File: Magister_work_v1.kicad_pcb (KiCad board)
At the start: 4 copper layers, 50.5 x 81 mm, 151 parts, among them J1 Conn_01x02_Pin, J10 Conn_01x06_Pin, J11 Conn_01x03_Pin, J12 Conn_01x03_Pin, J13 Conn_01x03_Pin, J14 Conn_01x03_Pin, J15 Conn_01x02_Pin, J17 Conn_01x04_Pin, J2 Conn_01x03_Pin, J3 Conn_01x03_Pin, J4 Conn_01x03_Pin, J5 Conn_01x03_Pin, J6 Conn_01x04_Pin, J7 Conn_01x02_Pin, J8 Conn_01x06_Pin, J9 Conn_01x02_Pin, Q1 AO3400A, Q2 AO3400A, U10 LSM6DS3, U11 MPU-6500, U12 BMI270, U2 XC6206P332MR, U3 Ai-Thinker-Ra-01, U4 MCP6001-OT, U5 AMS1117-3.3, U6 XL1509-5.0, U7 STM32F407VETx, U8 AT24C256, U9 Ai-Thinker-Ra-01SH, Y1 X322525MQB4SI, Y2 SMD03215C2

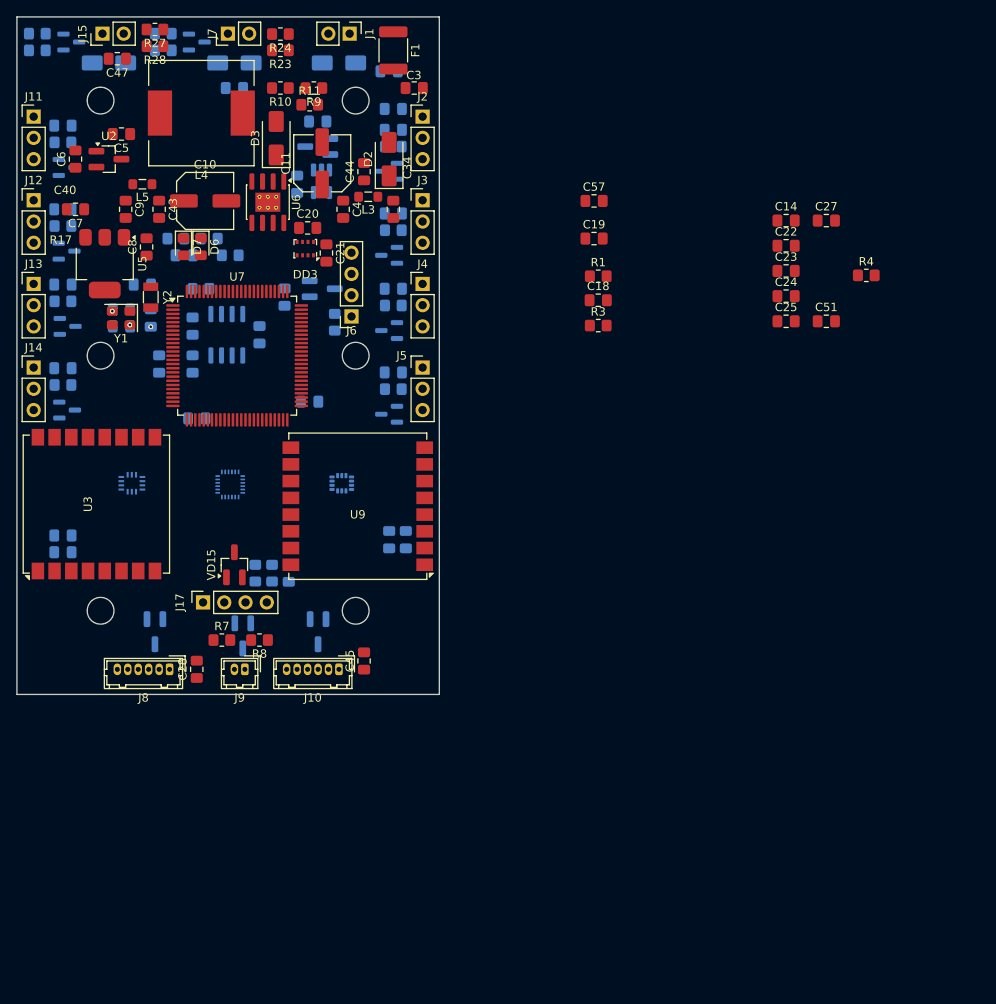
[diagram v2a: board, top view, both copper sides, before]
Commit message: feat: Разведены линии питания
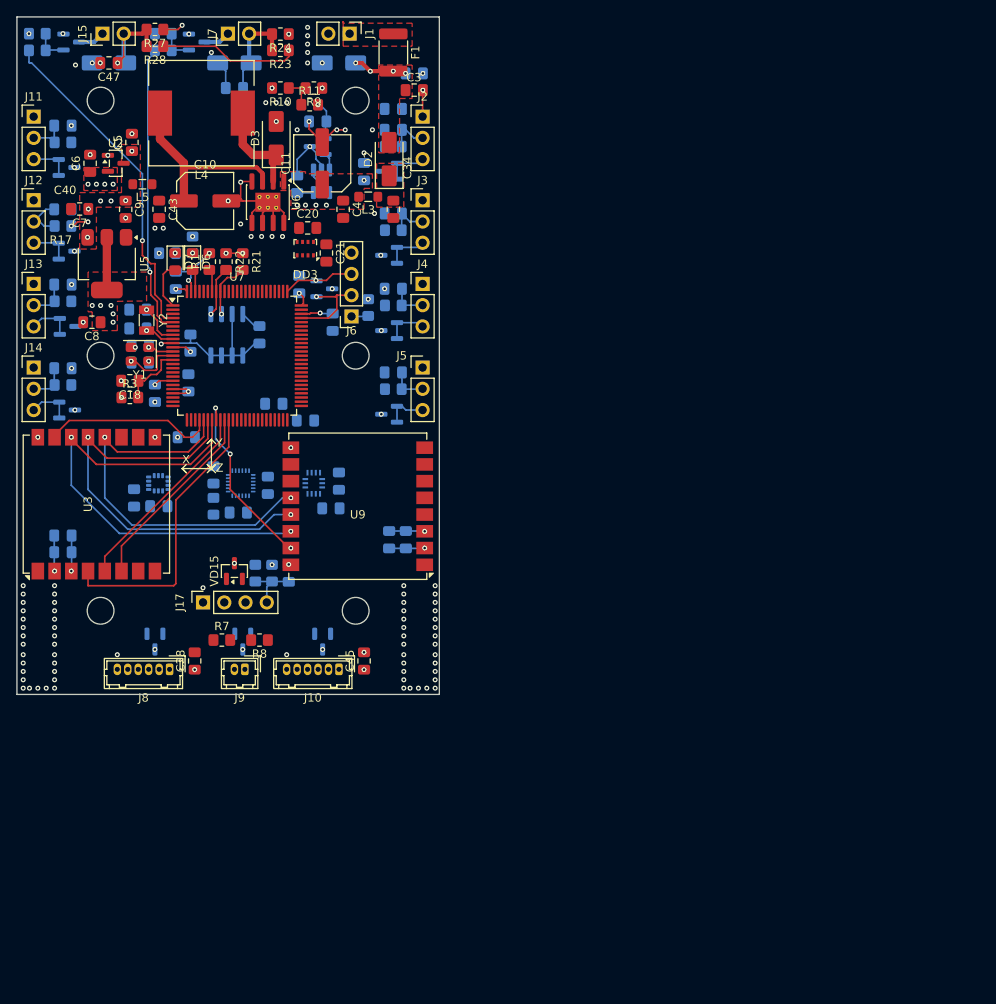
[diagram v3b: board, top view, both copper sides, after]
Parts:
- C14, C19, C22, C23, C24, C25, C27, C44, C51, C57, R4: moved to B.Cu
- R21, R22: moved to F.Cu
- U2, VD10, VD14, VD15, VD2, VD3, VD4: footprint Package_TO_SOT_SMD:SOT-23_Handsoldering -> Package_TO_SOT_SMD:SOT-23
- moved C22 83.6 mm to (44.0, 87.5), turned to -90 degrees
- moved R4 82.8 mm to (53.5, 88.5), turned to -90 degrees
- moved C23 80.1 mm to (47.0, 88.5)
- moved C25 70.9 mm to (53.5, 84.8), turned to 90 degrees
- moved C24 70.4 mm to (56.5, 89.2), turned to 180 degrees
- moved C14 69.6 mm to (60.0, 86.0), turned to 90 degrees
- moved C27 66.1 mm to (68.5, 85.5), turned to -90 degrees
- moved C51 63.3 mm to (67.5, 88.8), turned to 180 degrees
- moved C18 56.8 mm to (43.5, 73.5), turned to 180 degrees
- moved R3 56.7 mm to (43.5, 75.5)
- moved R1 46.5 mm to (53.0, 59.2), turned to 90 degrees
- moved C19 43.1 mm to (60.7, 76.2), turned to 180 degrees
- moved C57 34.5 mm to (67.8, 66.5), turned to -90 degrees
- moved U10 21.9 mm to (46.9, 85.8)
- moved U12 21.8 mm to (65.5, 85.8), turned to -90 degrees
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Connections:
- U6 pad 9: (no net) -> GND
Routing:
- net GND: track 0.00 -> 79.4 mm, vias 3 -> 133
- net MOSI_LoRa: track 0.00 -> 56.6 mm, vias 0 -> 2
- net MISO_LoRa: track 0.00 -> 51.9 mm, vias 0 -> 2
- net SCK_LoRa: track 0.00 -> 47.6 mm, vias 0 -> 2
- net POWER_DO2: track 0.00 -> 40.2 mm, vias 0 -> 1
- net +12V: track 0.00 -> 37.6 mm, vias 0 -> 7
- net +5V: track 0.00 -> 37.3 mm, vias 0 -> 13
- net POWER_DO1: track 0.00 -> 34.9 mm, vias 0 -> 1
- net Reset_LoRa: track 0.00 -> 34.5 mm
- net +3V3D: track 0.00 -> 27.3 mm, vias 0 -> 17
- net DIO0_LoRa: track 0.00 -> 23.8 mm
- net DIO1_LoRa: track 0.00 -> 23.2 mm
- net Net-(U6-FB): track 0.00 -> 22.9 mm
- net SS_RaSH: track 0.00 -> 22.1 mm, vias 0 -> 3
- net SS_LoRa: track 0.00 -> 20.8 mm
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- added copper zone on F.Cu, net +12V
- added copper zone on F.Cu, net +12V_1
- added copper zone on F.Cu, net +12V_in
- added copper zone on F.Cu, net +3V3A
- added copper zone on F.Cu, net +3V3D
- added copper zone on F.Cu, net +5V
- added copper zone on F.Cu, net Net-(D2-K)
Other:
- board text added: "X"
- board text added: "Y"
- board text added: "Z"

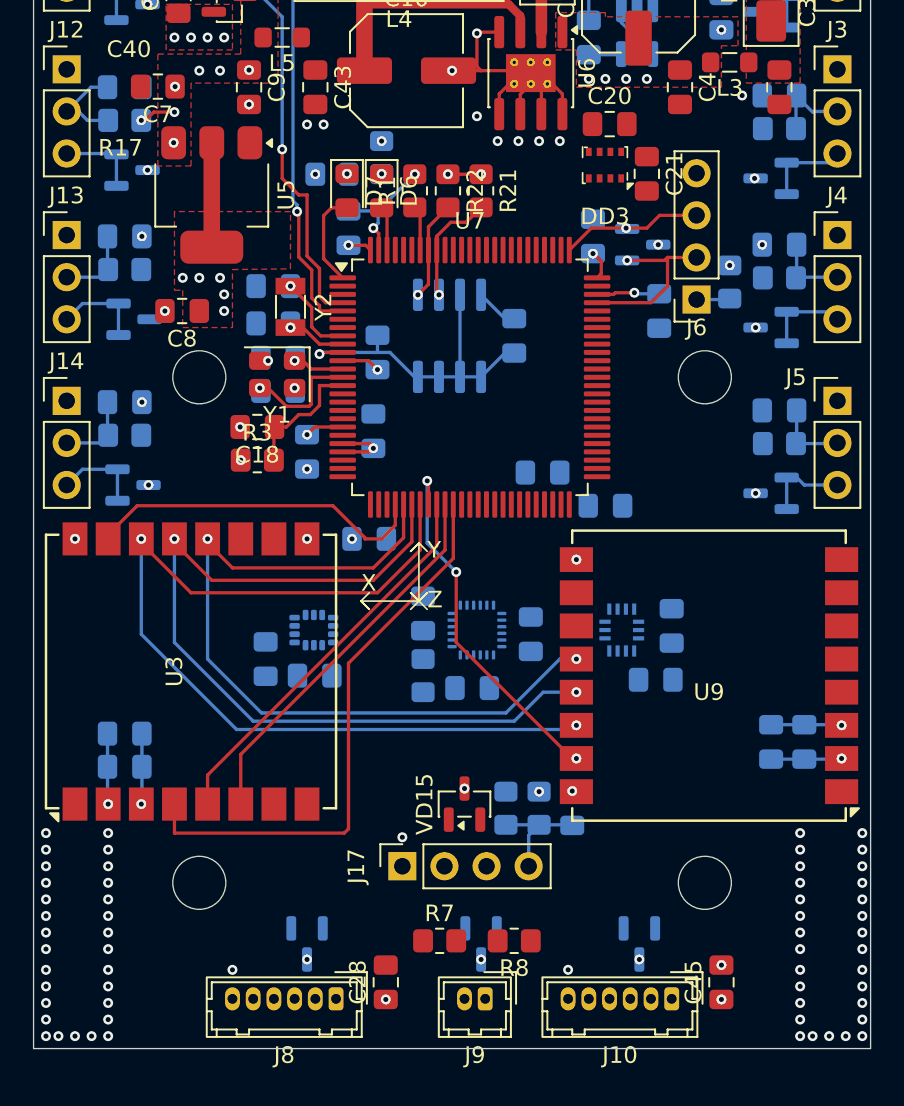
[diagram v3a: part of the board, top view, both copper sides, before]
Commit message: feat: разведены линии для датчиков LSM и BMP280
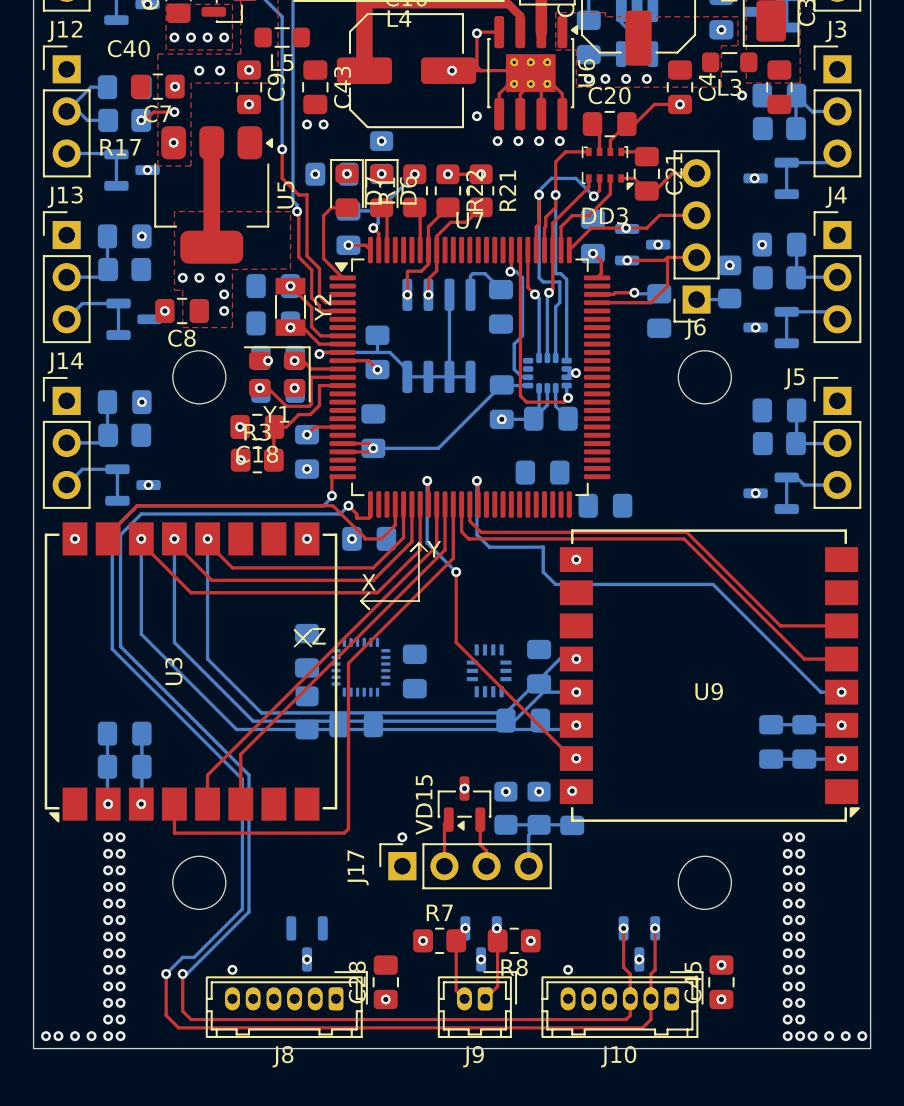
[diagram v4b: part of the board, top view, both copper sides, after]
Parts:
- moved C22 21.1 mm to (58.2, 72.0)
- moved C23 21.1 mm to (61.2, 73.0)
- moved U10 20.9 mm to (61.0, 70.2)
- moved C27 8.37 mm to (60.5, 88.0)
- moved U12 8.37 mm to (57.5, 88.2)
- moved C51 8.37 mm to (59.5, 91.2)
- moved C14 7.35 mm to (53.0, 88.2)
- moved C24 7.35 mm to (49.5, 91.5)
- moved C25 7.35 mm to (46.5, 87.0)
- moved R4 7.35 mm to (46.5, 90.8)
- moved U11 7.35 mm to (49.8, 88.0)
- moved C31 1.92 mm to (58.2, 66.2)
- moved U8 0.64 mm to (54.5, 68.0)
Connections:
- U6 pad 9: GND -> (no net)
- U7 pad 18: unconnected-(U7-PC3-Pad18) -> BAT_CTRL
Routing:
- net DEBUG_TX1: track 0.00 -> 86.2 mm, vias 0 -> 3
- net DEBUG_RX1: track 0.00 -> 83.5 mm, vias 0 -> 3
- net Reset_RaSH: track 0.00 -> 31.5 mm, vias 0 -> 2
- net DIO0_RaSH: track 0.00 -> 27.8 mm
- net DIO1_RaSH: track 0.00 -> 26.0 mm
- net LSM_SDI: track 0.00 -> 20.0 mm, vias 0 -> 2
- net LSM_SDO: track 0.00 -> 18.3 mm, vias 0 -> 1
- net GND: track 79.4 -> 95.3 mm, vias 133 -> 138
- net LSM_INT1: track 0.00 -> 12.7 mm, vias 0 -> 1
- net +3V3A: track 5.91 -> 18.5 mm
- net LSM_SCLK: track 0.00 -> 11.9 mm, vias 0 -> 1
- net LSM_INT2: track 0.00 -> 8.98 mm, vias 0 -> 1
- net LSM_CS: track 0.00 -> 6.79 mm, vias 0 -> 1
- net CSB_BMP280: track 0.00 -> 6.14 mm
- net +3V3D: track 27.3 -> 32.2 mm, vias 17 -> 20
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
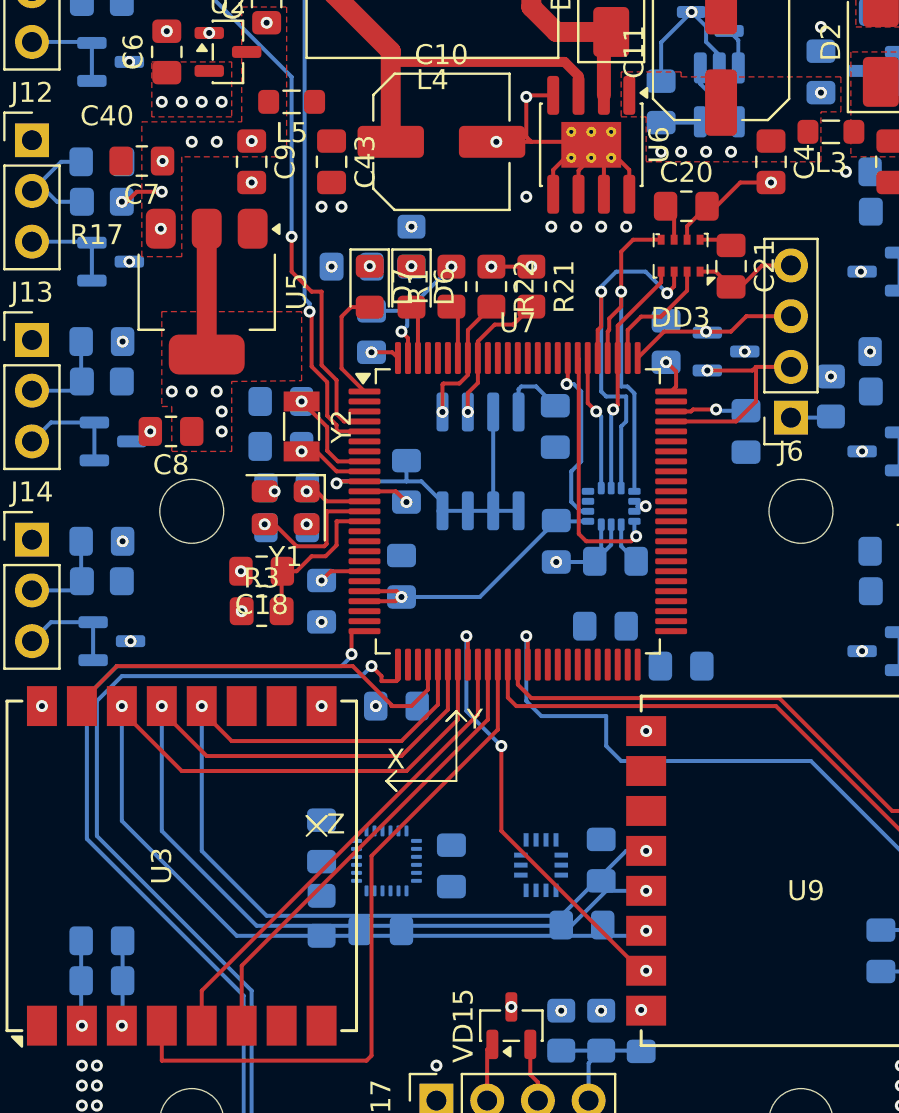
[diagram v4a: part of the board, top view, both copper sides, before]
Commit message: feat: Проведены цифровые линии от датчиков IMU
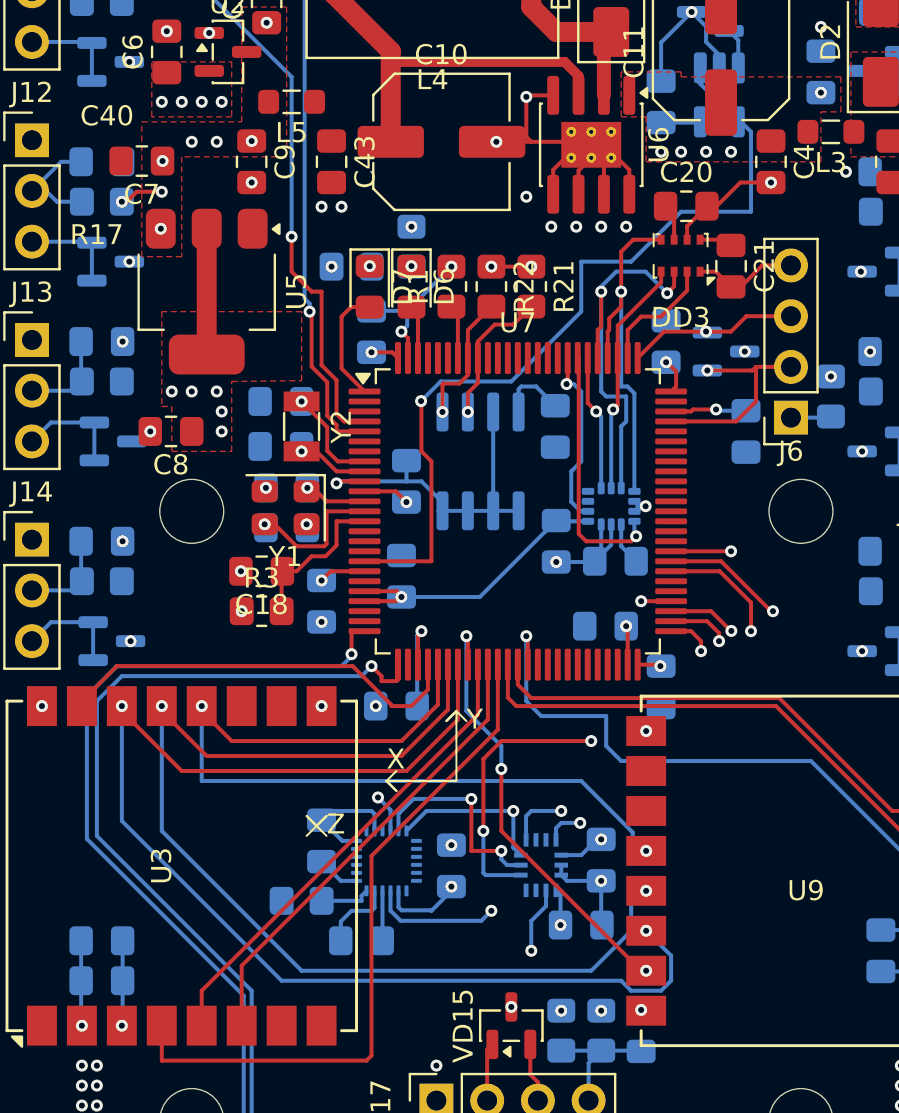
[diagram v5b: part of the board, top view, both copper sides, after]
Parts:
- moved C16 1.44 mm to (63.5, 79.3), turned to -90 degrees
- moved R4 1.25 mm to (45.5, 90.0), turned to 180 degrees
- moved C24 1.08 mm to (48.5, 92.0)
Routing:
- net MPU_CS: track 0.00 -> 48.0 mm, vias 0 -> 2
- net BAT_CTRL: track 3.49 -> 41.8 mm, vias 0 -> 1
- net BMI270_INT2: track 0.00 -> 36.8 mm, vias 0 -> 2
- net BMI270_SDO: track 0.00 -> 34.3 mm, vias 0 -> 3
- net BMI270_SCLK: track 0.00 -> 30.8 mm, vias 0 -> 3
- net BMI270_CS: track 0.00 -> 24.1 mm, vias 0 -> 3
- net BMI270_SDI: track 0.00 -> 23.7 mm, vias 0 -> 2
- net BMI270_INT1: track 0.00 -> 22.9 mm, vias 0 -> 2
- net GND: track 95.3 -> 109.9 mm, vias 138 -> 140
- net +3V3D: track 32.2 -> 45.4 mm, vias 20 -> 24
- net MOSI_LoRa: track 56.6 -> 62.1 mm
- net SCK_LoRa: track 47.6 -> 43.0 mm
- net +3V3A: track 18.5 -> 22.5 mm, vias 5 -> 6
- net MISO_LoRa: track 51.9 -> 54.7 mm
- net MPU_INT: track 0.00 -> 2.60 mm
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
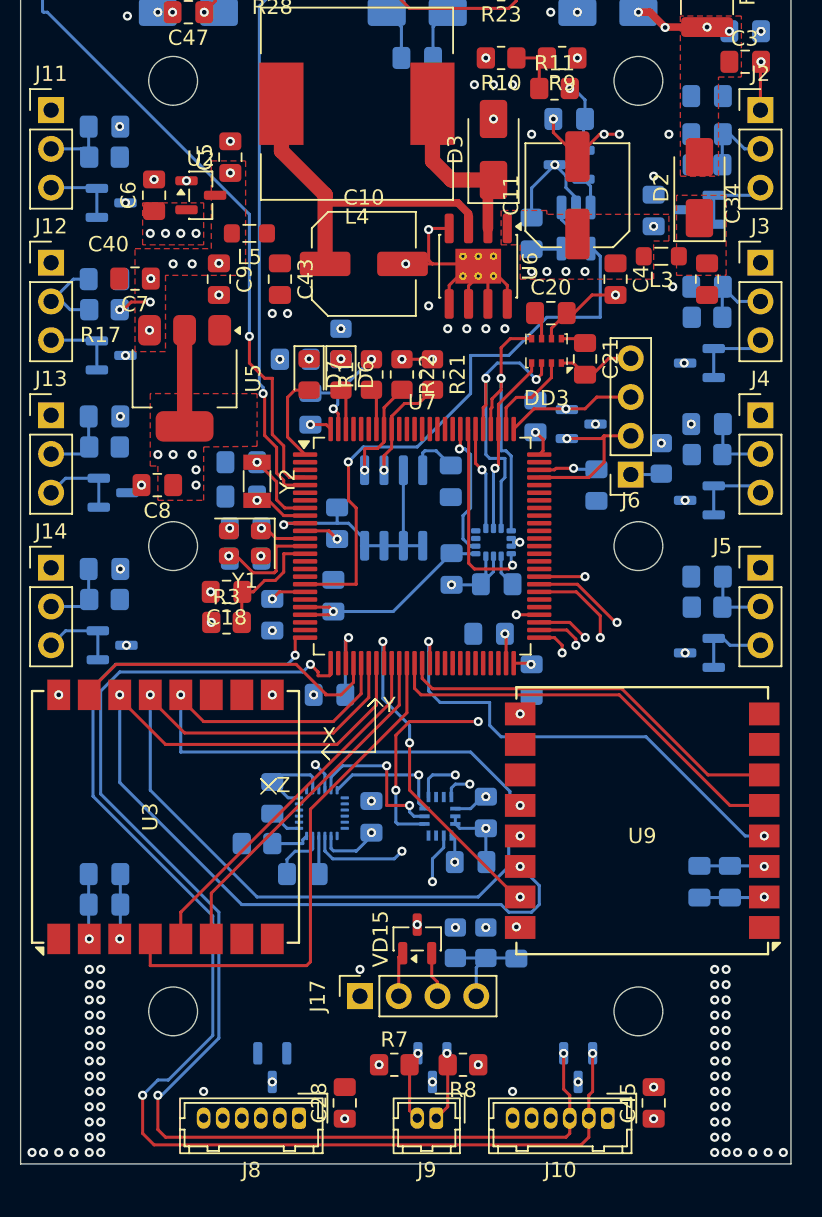
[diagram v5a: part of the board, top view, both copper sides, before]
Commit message: feat: Проведены линии для внешнего отладочного порта и внешенего компаса, провдена перекомпоновка разъёмов
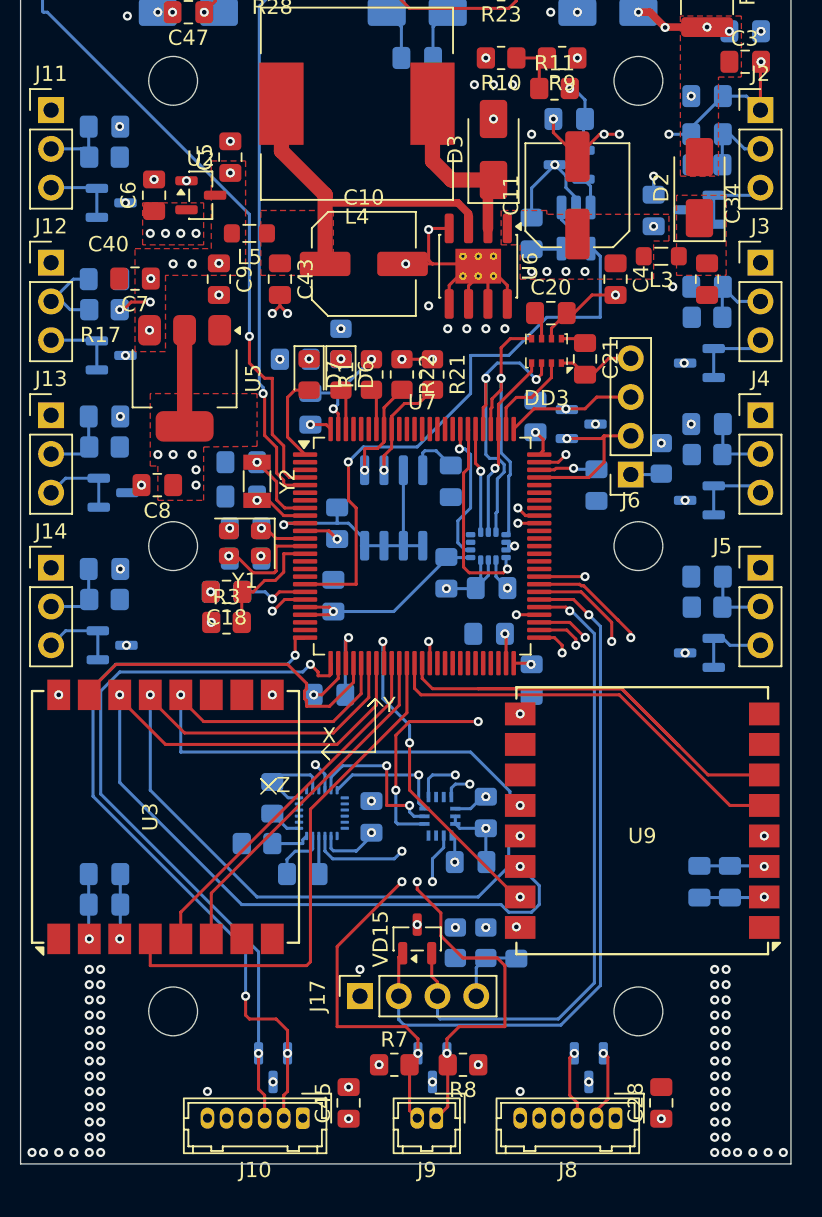
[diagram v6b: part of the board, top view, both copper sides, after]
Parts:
- moved C28 20.8 mm to (72.0, 107.0)
- moved J8 20.8 mm to (69.0, 108.0)
- moved VD2 20.8 mm to (67.2, 104.7)
- moved C45 20.0 mm to (51.5, 107.0)
- moved J10 20.0 mm to (48.5, 108.0)
- moved VD10 20.0 mm to (46.5, 104.7)
- moved C26 3.35 mm to (43.5, 73.5), turned to 180 degrees
- moved C22 0.42 mm to (57.9, 72.2)
- moved C23 0.42 mm to (60.9, 73.2)
- moved U10 0.42 mm to (60.7, 70.5)
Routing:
- net BN_880_SCL: track 4.68 -> 54.4 mm, vias 1 -> 3
- net BN_880_SDA: track 4.58 -> 53.3 mm, vias 1 -> 3
- net DEBUG_RX2: track 2.92 -> 47.2 mm, vias 0 -> 1
- net DEBUG_TX2: track 2.97 -> 42.9 mm, vias 0 -> 1
- net DEBUG_TX1: track 86.2 -> 50.6 mm
- net DEBUG_RX1: track 83.5 -> 49.5 mm, vias 3 -> 2
- net GND: track 109.9 -> 128.4 mm, vias 140 -> 141
- net DIO1_RaSH: track 26.0 -> 40.8 mm
- net BN_880_TX: track 0.00 -> 4.71 mm, vias 0 -> 1
- net BN_880_RX: track 0.00 -> 4.58 mm, vias 0 -> 1
- net +3V3D: track 45.4 -> 47.6 mm, vias 24 -> 25
- net SS_LoRa: track 20.8 -> 22.3 mm
- net Reset_RaSH: track 31.5 -> 30.5 mm
- net BMI270_INT2: track 36.8 -> 37.6 mm
- net MPU_CS: track 48.0 -> 48.9 mm
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- added copper zone on F.Cu, net Net-(U6-FB)
